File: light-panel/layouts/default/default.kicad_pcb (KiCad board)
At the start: 2 copper layers, 150 x 25 mm, 66 parts

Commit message: v1 of flat panel
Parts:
- added INPUT: , HanElectricity_2541WV_06P:HDR-TH_6P-P2.54-V-M, F.Cu at (51.6, 111.5)
- added OUTPUT: , HanElectricity_2541WV_06P:HDR-TH_6P-P2.54-V-M, F.Cu at (198.3, 111.5)
- R1, R4: footprint UNI_ROYAL_0402WGF6801TCE:R0402 -> UNI_ROYAL_0603WAF6801T5E:R0603
- moved R1 89.6 mm to (90.9, 110.1), turned to 180 degrees
- moved C2 86.0 mm to (90.9, 113.8)
- moved R3 85.3 mm to (90.9, 111.9)
- moved C3 63.0 mm to (95.4, 114.7), turned to 180 degrees
- moved R4 46.3 mm to (160.9, 110.1), turned to 180 degrees
- moved R2 44.5 mm to (105.3, 111.9)
- moved C4 38.4 mm to (160.9, 113.8)
- moved R6 37.0 mm to (160.9, 111.9)
- moved R15 35.9 mm to (119.6, 119.9), turned to -90 degrees
- moved R22 35.7 mm to (187.7, 119.9), turned to 90 degrees
- moved R13 35.1 mm to (61.3, 119.4), turned to -90 degrees
- moved R24 34.5 mm to (111.7, 119.6), turned to 90 degrees
- moved R21 34.2 mm to (189.5, 119.9), turned to -90 degrees
- moved R12 34.0 mm to (189.1, 105.0), turned to -90 degrees
- moved R16 33.9 mm to (121.3, 119.9), turned to 90 degrees
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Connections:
- net ballast[0]-input renamed warm_led-1
- net ballast[2]-input renamed warm_led-1-2
- net ballast[4]-input renamed warm_led-1-4
- net ballast[6]-input renamed warm_led-1-6
- net ballast[8]-input renamed warm_led-1-8
- net channel-input renamed warm_led-A
- net cool_led-ballast[1]-input renamed cool_led-1
- net cool_led-ballast[3]-input renamed cool_led-1-2
- net cool_led-ballast[5]-input renamed cool_led-1-4
- net cool_led-ballast[7]-input renamed cool_led-1-6
- net cool_led-ballast[9]-input renamed cool_led-1-8
- net cool_led-leds[11]-input renamed cool_led-1-5
- net cool_led-leds[11]-input-1 renamed cool_led-A-1
- net cool_led-leds[14]-input renamed cool_led-1-7
- net cool_led-leds[14]-input-1 renamed cool_led-A-4
- net cool_led-leds[2]-input renamed cool_led-A-5
- net cool_led-leds[5]-input renamed cool_led-1-1
- net cool_led-leds[5]-input-1 renamed cool_led-A-7
- net cool_led-leds[8]-input renamed cool_led-1-3
- net cool_led-leds[8]-input-1 renamed cool_led-A-9
- net cool_led-leds[9]-input renamed A
- net cool_led-leds[9]-input-1 renamed cool_led-A-2
- net input_cap-power-hv renamed V+
- net led-input renamed warm_led-A-1
- net led-input-1 renamed warm_led-A-3
- net led-input-2 renamed warm_led-A-2
- net led-input-3 renamed warm_led-A-4
- net led-input-4 renamed warm_led-A-5
- net led-input-5 renamed warm_led-A-6
- net led-input-6 renamed warm_led-A-7
- net led-input-7 renamed warm_led-A-8
- net led-input-8 renamed warm_led-A-9
- net led-input-9 renamed warm_led-A-10
- net leds[13]-input renamed cool_led-A-3
- net leds[1]-input renamed cool_led-A
- net leds[4]-input renamed cool_led-A-6
- net leds[7]-input renamed cool_led-A-8
- net lv renamed GND
- net output renamed 2
- net warm_led-ballast[1]-input renamed warm_led-1-1
- net warm_led-ballast[3]-input renamed warm_led-1-3
- net warm_led-ballast[5]-input renamed warm_led-1-5
- net warm_led-ballast[7]-input renamed warm_led-1-7
- net warm_led-ballast[9]-input renamed warm_led-1-9
- net warm_led-ballast[9]-output renamed warm_led-2
- D1 pad 1: 1 -> cool_led.channel-1
- L1 pad 2: 1 -> cool_led.channel-1
- LED_C_1_3 pad 1: input -> 1
- R1 pad 1: cool_pwm -> pwm_cool
- R4 pad 1: warm_pwm -> pwm_warm
- R7 pad 1: input -> 1
- U1 pad 1: 1 -> cool_led.channel-1
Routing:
- net warm_led-A: track 0.00 -> 204.3 mm, vias 0 -> 4
- net 2: track 0.00 -> 191.6 mm, vias 0 -> 6
- net V+: track 0.00 -> 172.8 mm
- net warm_led-2: track 0.00 -> 164.4 mm, vias 0 -> 2
- net pwm_cool: track 0.00 -> 161.8 mm, vias 0 -> 3
- net A: track 0.00 -> 150.8 mm, vias 0 -> 8
- net pwm_warm: track 0.00 -> 150.1 mm, vias 0 -> 2
- net cool_led.channel-1: track 0.00 -> 38.3 mm
- net warm_led.channel-1: track 0.00 -> 37.5 mm, vias 0 -> 2
- net cool_led-A-2: track 0.00 -> 26.5 mm, vias 0 -> 2
- net cool_led-A-4: track 0.00 -> 26.2 mm, vias 0 -> 2
- net cool_led-A-8: track 0.00 -> 25.6 mm
- net cool_led-A: track 0.00 -> 25.4 mm
- net cool_led-A-1: track 0.00 -> 25.0 mm
- net cool_led-A-3: track 0.00 -> 25.0 mm
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- added copper zone on B.Cu, net GND
- added copper zone on F.Cu, net GND

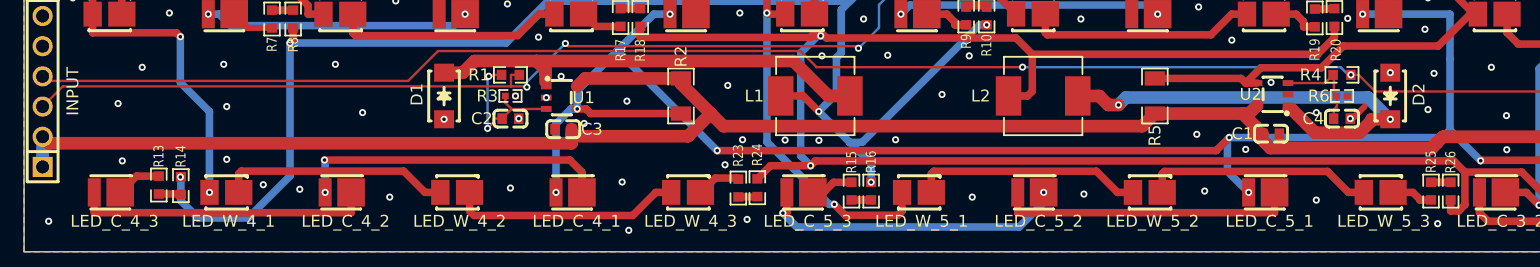
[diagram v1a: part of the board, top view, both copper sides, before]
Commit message: minor panel improvements
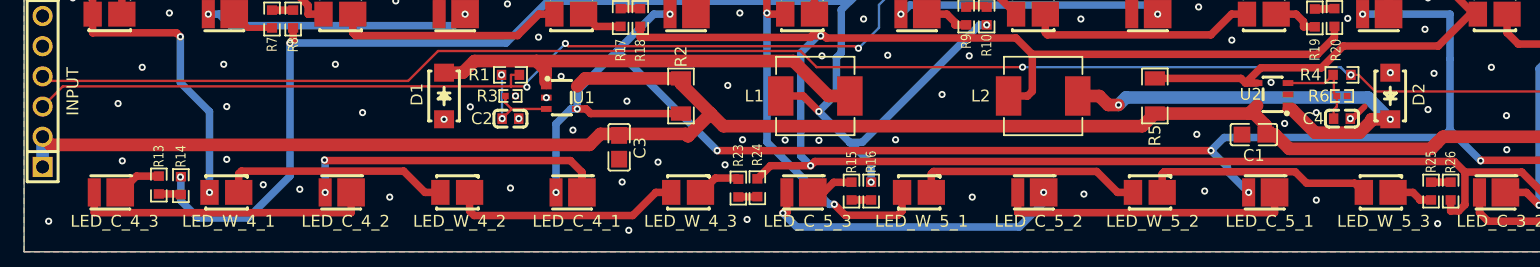
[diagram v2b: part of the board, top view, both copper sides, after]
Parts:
- C1, C3: footprint Samsung_Electro_Mechanics_CL10A106KP8NNNC:C0603 -> Murata_Electronics_GRM21BR61H106KE43L:C0805
- moved C3 4.94 mm to (100.1, 116.2), turned to -90 degrees
- moved C1 1.45 mm to (153.5, 115.1), turned to 180 degrees
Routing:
- net hv: track 12.8 -> 9.24 mm
- net V+: track 172.8 -> 170.9 mm
- net A: track 150.8 -> 150.2 mm
- net GND: vias 77 -> 79

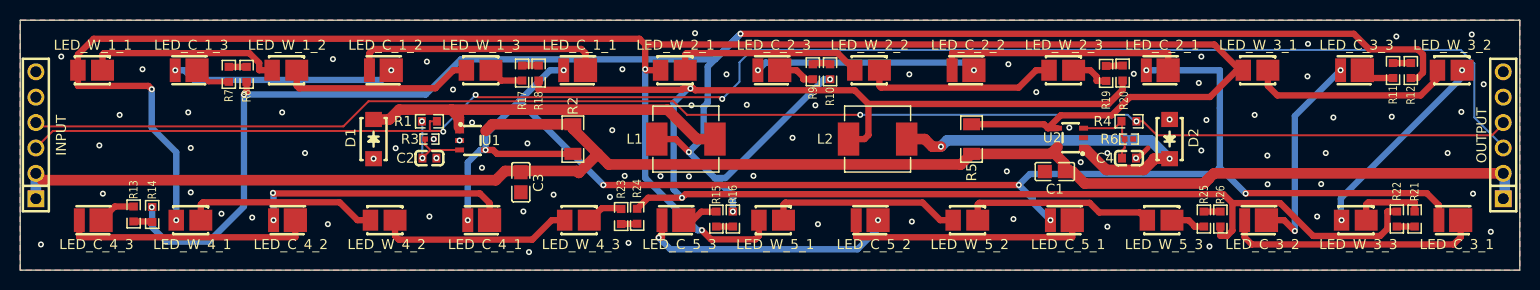
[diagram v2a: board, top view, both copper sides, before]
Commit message: switched led inductors
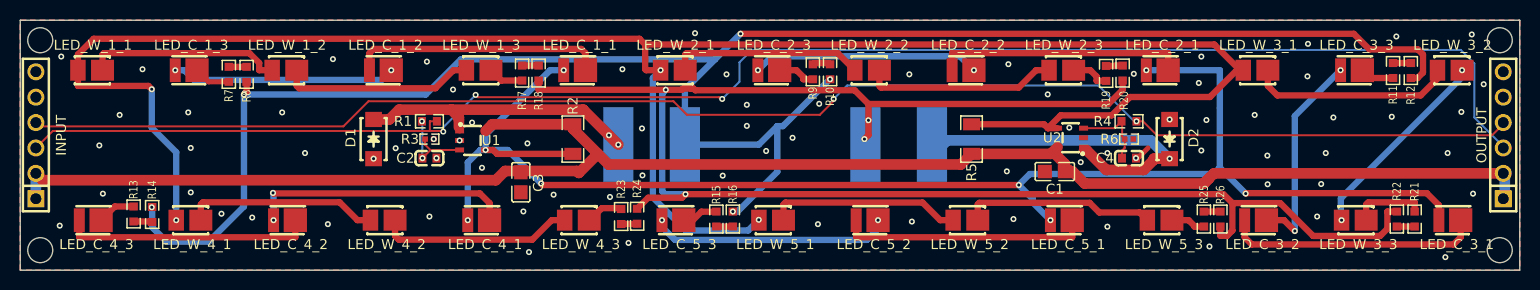
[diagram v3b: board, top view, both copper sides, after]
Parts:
- L1, L2: footprint SXN_SMMS0650_680M:IND-SMD_L7.1-W6.6_H5.0 -> BOURNS_SRN8040TA_680M:IND-SMD_L8.0-W8.0; moved to B.Cu
- moved L1 3.47 mm to (113.2, 112.4)
- moved L2 2.18 mm to (137.9, 112.4), turned to 180 degrees
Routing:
- net cool_led.channel-1: track 38.3 -> 28.8 mm, vias 0 -> 2
- net warm_led.channel-1: track 37.5 -> 33.8 mm, vias 2 -> 1
- net 2: track 191.6 -> 188.1 mm, vias 6 -> 5
- net pwm_warm: track 150.1 -> 152.6 mm
- net cool_led-A-4: track 26.2 -> 24.1 mm
- net cool_led-1-7: track 3.62 -> 4.99 mm
- net A: track 150.2 -> 151.5 mm
- net warm_led-A: track 204.3 -> 203.2 mm
- net warm_led-2: track 164.4 -> 163.4 mm, vias 2 -> 4
- net cool_led-A-7: track 22.2 -> 22.8 mm
- net GND: vias 79 -> 78
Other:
- outline, holes or cut-outs redrawn

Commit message: Panel Cleanup
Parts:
- added REF**: KiCad-Logo2_5mm_SilkScreen, Symbol:KiCad-Logo2_5mm_SilkScreen, F.Cu at (65.4, 111.8)
- added REF**: OSHW-Logo_7.5x8mm_SilkScreen, Symbol:OSHW-Logo_7.5x8mm_SilkScreen, F.Cu at (77.5, 112.4)
- + H1 -: renamed from INPUT; footprint HanElectricity_2541WV_06P:HDR-TH_6P-P2.54-V-M -> BOOMELE_2_54_2_3P:HDR-TH_6P-P2.54-V-M-R2-C3-S2.54-1
- + H2 -: renamed from OUTPUT; footprint HanElectricity_2541WV_06P:HDR-TH_6P-P2.54-V-M -> BOOMELE_2_54_2_3P:HDR-TH_6P-P2.54-V-M-R2-C3-S2.54-1
- moved R21 1.78 mm to (187.7, 119.9), turned to 90 degrees
- moved R22 1.78 mm to (189.5, 119.9), turned to -90 degrees
- moved + H1 - 1.75 mm to (53.0, 112.5)
- moved + H2 - 1.68 mm to (197.0, 112.5)
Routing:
- net V+: track 170.9 -> 330.2 mm
- net warm_led-1-4: track 7.43 -> 3.34 mm
- net pwm_warm: track 152.6 -> 150.2 mm
- net pwm_cool: track 161.8 -> 163.4 mm
- net GND: track 1.63 -> 2.37 mm, vias 78 -> 76
- added copper zone on F.Cu, net V+
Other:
- board size 150 x 25 mm -> 150 x 29.7 mm

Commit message: panel router
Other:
- board size 150 x 29.7 mm -> 150 x 30 mm
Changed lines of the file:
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@@
 	)
 	(gr_circle
-		(center 52 99.25)
-		(end 53.25 99.25)
+		(center 52 99.5)
+		(end 53.25 99.5)
 		(stroke
 			(width 0.05)
@@
 	)
 	(gr_circle
-		(center 198 99.25)
-		(end 199.25 99.25)
+		(center 198 99.5)
+		(end 199.25 99.5)
 		(stroke
 			(width 0.05)
@@
 	)
 	(gr_circle
-		(center 198 125.25)
-		(end 199.25 125.25)
+		(center 198 125.5)
+		(end 199.25 125.5)
 		(stroke
 			(width 0.05)
@@
 	(gr_rect
 		(start 50 97.5)
-		(end 200 127.2)
+		(end 200 127.5)
 		(stroke
 			(width 0.05)
@@
 	)
 	(gr_circle
-		(center 52 125.25)
-		(end 53.25 125.25)
+		(center 52 125.5)
+		(end 53.25 125.5)
 		(stroke
 			(width 0.05)

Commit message: Cleanup
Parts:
- REF**: moved to B.Cu
- moved REF** 120.0 mm to (185.1, 119.8), turned to 180 degrees

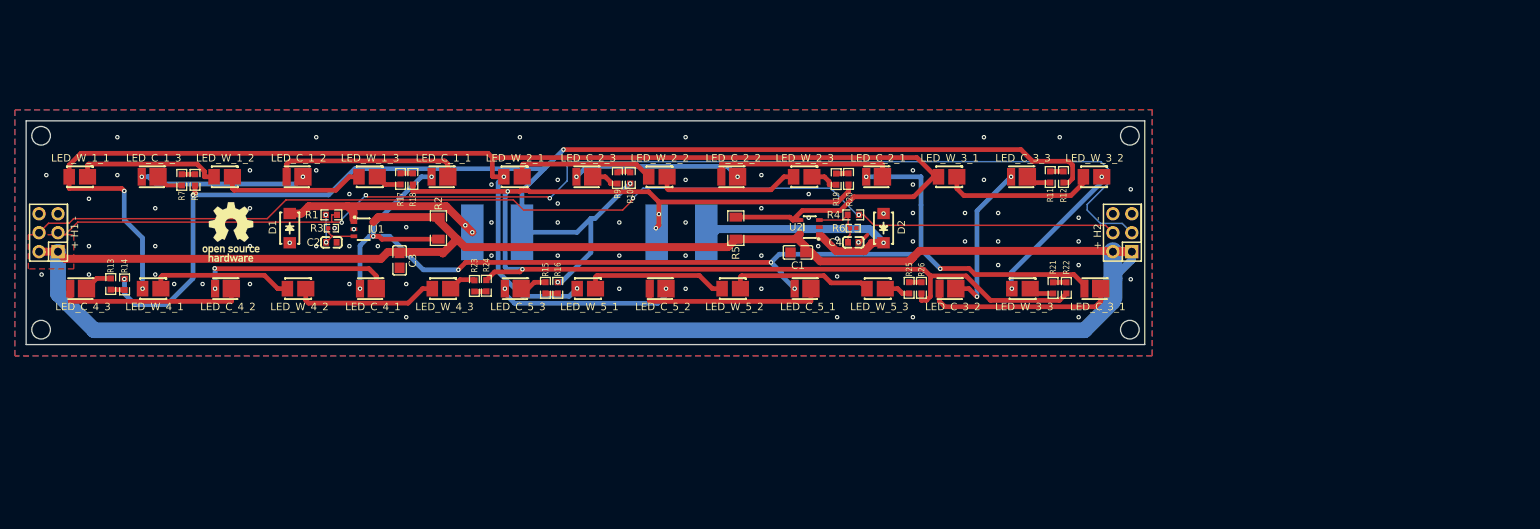
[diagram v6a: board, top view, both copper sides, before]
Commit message: Updated LED Panel Headers
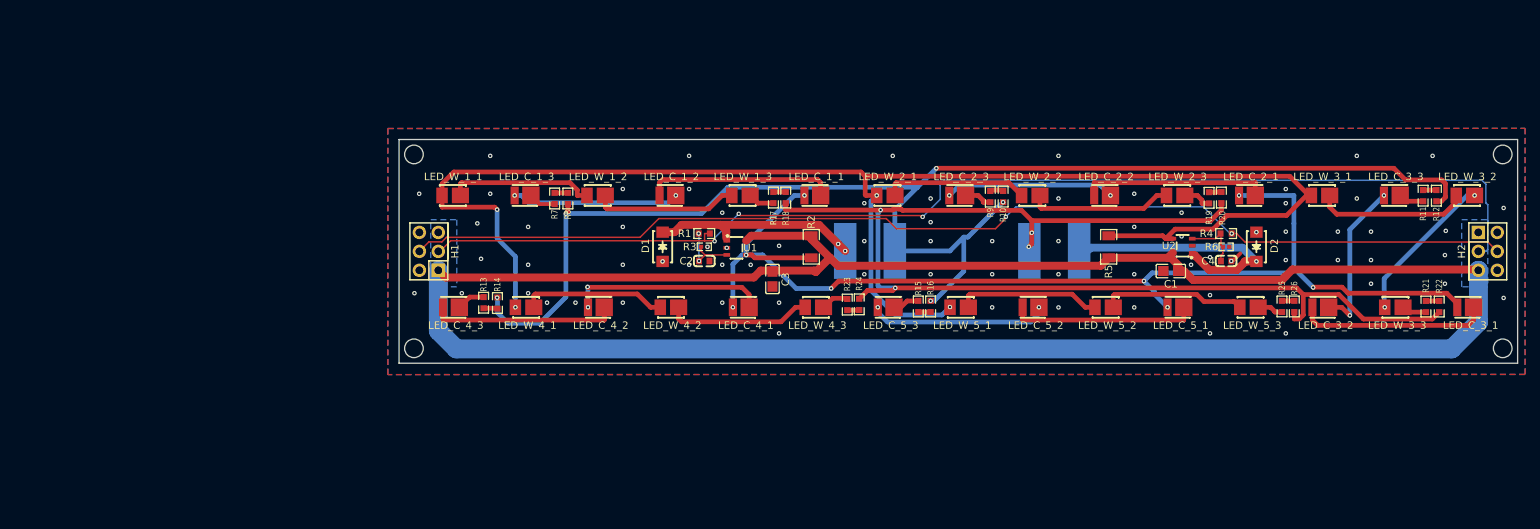
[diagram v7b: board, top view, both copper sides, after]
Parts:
- removed REF**: OSHW-Logo_7.5x8mm_SilkScreen, Symbol:OSHW-Logo_7.5x8mm_SilkScreen
- removed REF**: KiCad-Logo2_5mm_SilkScreen, Symbol:KiCad-Logo2_5mm_SilkScreen
- H1: renamed from + H1 -
- H2: renamed from + H2 -
- moved H1 51.1 mm to (104.0, 115.0)
- moved L1 50.1 mm to (163.2, 114.9)
- moved R18 50.1 mm to (151.9, 107.8)
- moved R23 50.1 mm to (160.1, 122.1)
- moved R24 50.1 mm to (161.7, 122.1)
- moved C1 50.1 mm to (203.5, 117.6)
- moved C3 50.1 mm to (150.1, 118.7)
- moved C4 50.1 mm to (210.9, 116.3)
- moved D1 50.1 mm to (135.3, 114.4)
- moved D2 50.1 mm to (215.0, 114.4)
- moved L2 50.1 mm to (187.9, 114.9)
- moved LED_C_1_1 50.1 mm to (155.5, 107.5)
- moved LED_C_1_3 50.1 mm to (116.6, 107.5)
- moved LED_C_2_1 50.1 mm to (213.7, 107.5)
- moved LED_C_2_2 50.1 mm to (194.3, 107.5)
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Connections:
- H1 pad 2: V+ -> GND
- H1 pad 5: GND -> V+
- H2 pad 2: V+ -> GND
- H2 pad 5: GND -> V+
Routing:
- net V+: track 330.2 -> 316.0 mm
- net pwm_cool: track 163.4 -> 158.2 mm
- net GND: track 2.37 -> 1.63 mm, vias 76 -> 75
- net warm_led-A-10: track 20.1 -> 20.6 mm
- net pwm_warm: track 150.2 -> 150.7 mm
- added copper zone on B.Cu, net V+
- removed copper zone on F.Cu, net V+
